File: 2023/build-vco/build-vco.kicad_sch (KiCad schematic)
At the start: 5 parts, among them M1 PMOS_OR1, M2 NMOS_OR1, M27 NMOS_OR1, M3 PMOS_OR1, M4 NMOS_OR1

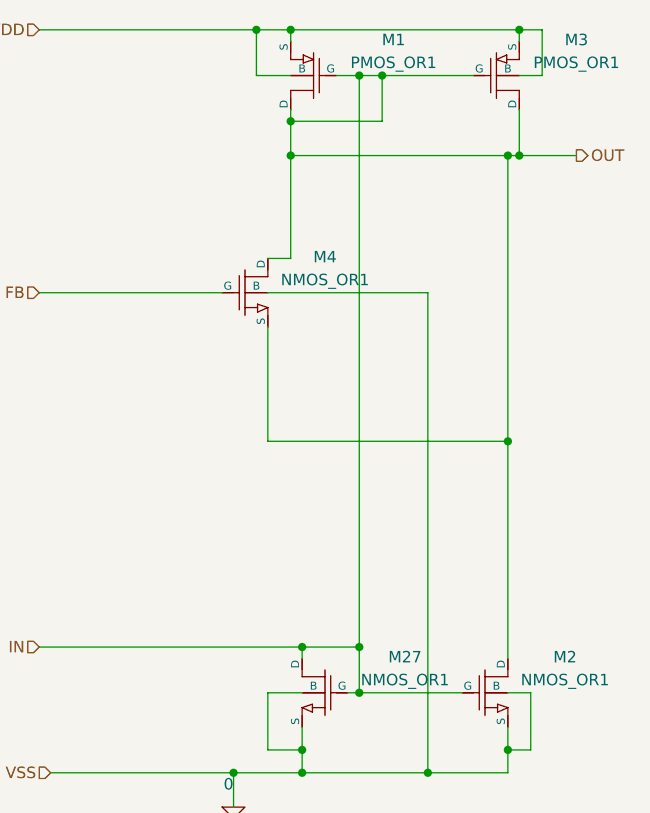
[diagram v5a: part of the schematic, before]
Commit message: 二本信号線を削った。
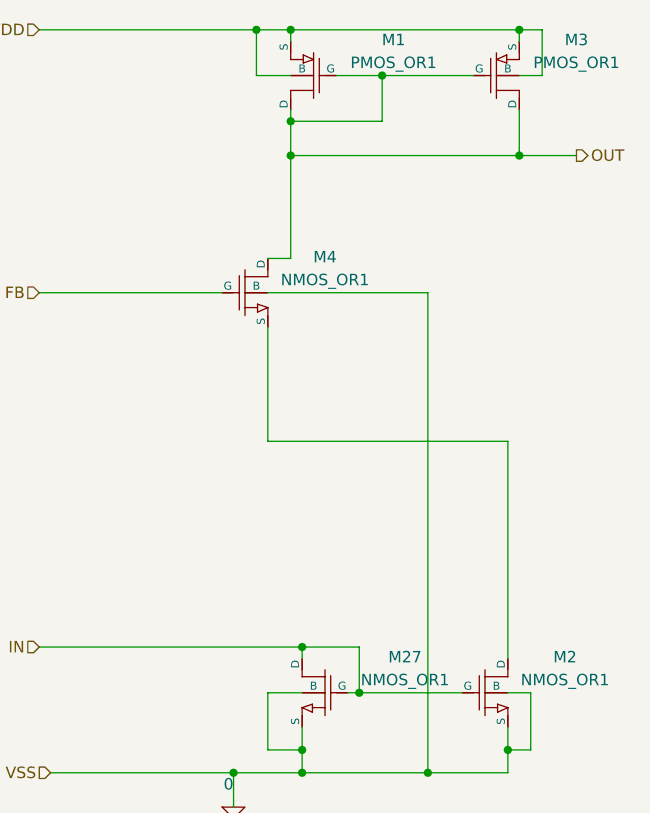
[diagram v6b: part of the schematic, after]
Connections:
- net IN: no longer M1.1 (D), M1.2 (G), M2.1 (D), M3.1 (D), M3.2 (G), M4.1 (D), M4.3 (S)
- new net: M2.1 (D), M4.3 (S)
- new net OUT: M1.1 (D), M1.2 (G), M3.1 (D), M3.2 (G), M4.1 (D)
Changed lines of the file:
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@@
   (junction (at 156.21 134.62) (diameter 0) (color 0 0 0 0)
-  )
-  (junction (at 139.7 59.69) (diameter 0) (color 0 0 0 0)
-  )
-  (junction (at 156.21 68.58) (diameter 0) (color 0 0 0 0)
-  )
-  (junction (at 156.21 100.33) (diameter 0) (color 0 0 0 0)
   )
   (junction (at 142.24 59.69) (diameter 0) (color 0 0 0 0)
@@
   )
   (junction (at 139.7 128.27) (diameter 0) (color 0 0 0 0)
-  )
-  (junction (at 139.7 123.19) (diameter 0) (color 0 0 0 0)
   )
   (junction (at 132.08 64.77) (diameter 0) (color 0 0 0 0)
@@
     (stroke (width 0) (type default))
   )
-  (wire (pts (xy 139.7 59.69) (xy 139.7 123.19))
-    (stroke (width 0) (type default))
-  )
-  (wire (pts (xy 156.21 68.58) (xy 157.48 68.58))
+  (wire (pts (xy 132.08 68.58) (xy 157.48 68.58))
     (stroke (width 0) (type default))
   )
@@
   )
   (wire (pts (xy 129.54 80.01) (xy 132.08 80.01))
-    (stroke (width 0) (type default))
-  )
-  (wire (pts (xy 137.16 59.69) (xy 139.7 59.69))
     (stroke (width 0) (type default))
   )
@@
     (stroke (width 0) (type default))
   )
-  (wire (pts (xy 139.7 59.69) (xy 142.24 59.69))
+  (wire (pts (xy 137.16 59.69) (xy 142.24 59.69))
     (stroke (width 0) (type default))
   )
@@
     (stroke (width 0) (type default))
   )
-  (wire (pts (xy 156.21 68.58) (xy 156.21 100.33))
-    (stroke (width 0) (type default))
-  )
   (wire (pts (xy 156.21 137.16) (xy 147.32 137.16))
     (stroke (width 0) (type default))
   )
-  (wire (pts (xy 132.08 68.58) (xy 156.21 68.58))
-    (stroke (width 0) (type default))
-  )

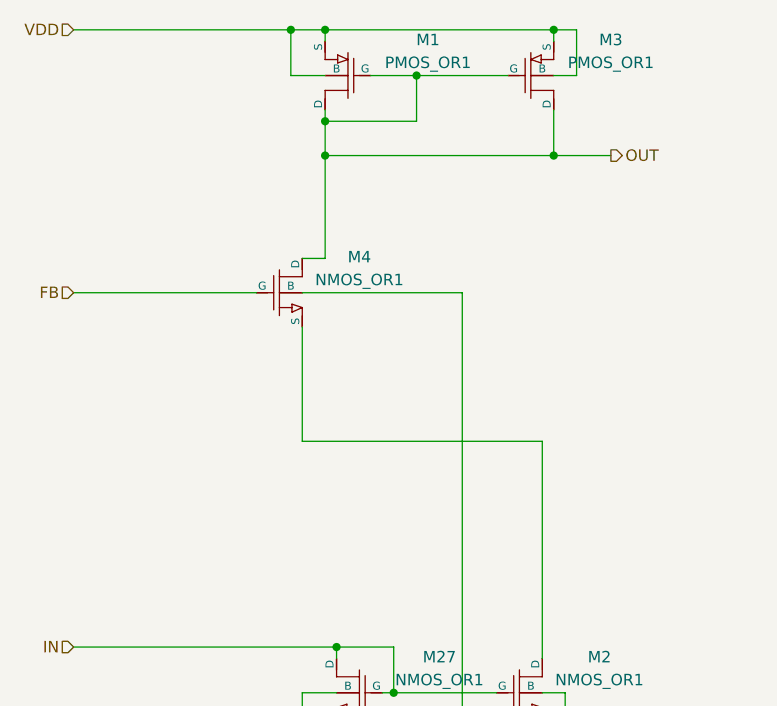
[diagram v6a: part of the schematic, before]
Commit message: PMOS x 2, NMOS x 5 で LVS は OK.
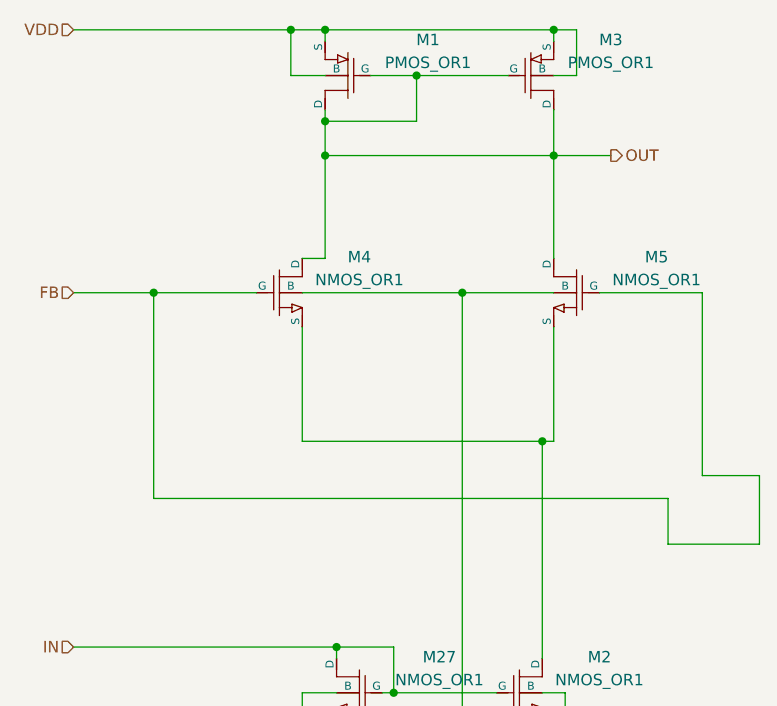
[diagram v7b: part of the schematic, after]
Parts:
- added M5: NMOS_OR1, symbol OR1Symbols:NMOS_OR1
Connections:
- net 0: now also M5.4 (B)
- net FB: now also M5.2 (G)
- net OUT: now also M5.1 (D)
- net at M2.1 (D), M4.3 (S): now also M5.3 (S)
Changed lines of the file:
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@@
   (junction (at 156.21 134.62) (diameter 0) (color 0 0 0 0)
   )
+  (junction (at 113.03 83.82) (diameter 0) (color 0 0 0 0)
+  )
+  (junction (at 147.32 83.82) (diameter 0) (color 0 0 0 0)
+  )
   (junction (at 142.24 59.69) (diameter 0) (color 0 0 0 0)
   )
@@
   (junction (at 133.35 134.62) (diameter 0) (color 0 0 0 0)
   )
+  (junction (at 156.21 100.33) (diameter 0) (color 0 0 0 0)
+  )
   (junction (at 128.27 54.61) (diameter 0) (color 0 0 0 0)
   )
@@
   (junction (at 125.73 137.16) (diameter 0) (color 0 0 0 0)
   )
+  (wire (pts (xy 147.32 83.82) (xy 157.48 83.82))
+    (stroke (width 0) (type default))
+  )
   (wire (pts (xy 104.14 54.61) (xy 128.27 54.61))
     (stroke (width 0) (type default))
@@
     (stroke (width 0) (type default))
   )
+  (wire (pts (xy 180.34 104.14) (xy 180.34 111.76))
+    (stroke (width 0) (type default))
+  )
   (wire (pts (xy 132.08 68.58) (xy 132.08 80.01))
     (stroke (width 0) (type default))
@@
     (stroke (width 0) (type default))
   )
+  (wire (pts (xy 113.03 106.68) (xy 170.18 106.68))
+    (stroke (width 0) (type default))
+  )
   (wire (pts (xy 157.48 54.61) (xy 160.02 54.61))
     (stroke (width 0) (type default))
@@
     (stroke (width 0) (type default))
   )
+  (wire (pts (xy 173.99 83.82) (xy 173.99 104.14))
+    (stroke (width 0) (type default))
+  )
   (wire (pts (xy 129.54 128.27) (xy 129.54 134.62))
     (stroke (width 0) (type default))
@@
     (stroke (width 0) (type default))
   )
+  (wire (pts (xy 162.56 83.82) (xy 173.99 83.82))
+    (stroke (width 0) (type default))
+  )
   (wire (pts (xy 125.73 137.16) (xy 133.35 137.16))
     (stroke (width 0) (type default))
@@
     (stroke (width 0) (type default))
   )
+  (wire (pts (xy 170.18 111.76) (xy 170.18 106.68))
+    (stroke (width 0) (type default))
+  )
   (wire (pts (xy 132.08 64.77) (xy 132.08 68.58))
     (stroke (width 0) (type default))
   )
-  (wire (pts (xy 104.14 83.82) (xy 124.46 83.82))
+  (wire (pts (xy 104.14 83.82) (xy 113.03 83.82))
     (stroke (width 0) (type default))
   )
@@
     (stroke (width 0) (type default))
   )
+  (wire (pts (xy 157.48 87.63) (xy 157.48 100.33))
+    (stroke (width 0) (type default))
+  )
   (wire (pts (xy 157.48 68.58) (xy 163.83 68.58))
     (stroke (width 0) (type default))
@@
     (stroke (width 0) (type default))
   )
+  (wire (pts (xy 113.03 106.68) (xy 113.03 83.82))
+    (stroke (width 0) (type default))
+  )
   (wire (pts (xy 157.48 59.69) (xy 160.02 59.69))
     (stroke (width 0) (type default))
   )
+  (wire (pts (xy 180.34 111.76) (xy 170.18 111.76))
+    (stroke (width 0) (type default))
+  )
   (wire (pts (xy 142.24 59.69) (xy 142.24 64.77))
     (stroke (width 0) (type default))
@@
     (stroke (width 0) (type default))
   )
+  (wire (pts (xy 157.48 68.58) (xy 157.48 80.01))
+    (stroke (width 0) (type default))
+  )
+  (wire (pts (xy 173.99 104.14) (xy 180.34 104.14))
+    (stroke (width 0) (type default))
+  )
   (wire (pts (xy 142.24 59.69) (xy 152.4 59.69))
     (stroke (width 0) (type default))
@@
     (stroke (width 0) (type default))
   )
+  (wire (pts (xy 156.21 100.33) (xy 157.48 100.33))
+    (stroke (width 0) (type default))
+  )
   (wire (pts (xy 132.08 63.5) (xy 132.08 64.77))
+    (stroke (width 0) (type default))
+  )
+  (wire (pts (xy 113.03 83.82) (xy 124.46 83.82))
     (stroke (width 0) (type default))
   )
@@
         )
       )
+    )
+  )
+  (symbol (lib_name "NMOS_OR1_3") (lib_id "OR1Symbols:NMOS_OR1") (at 162.56 83.82 0) (mirror y) (unit 1)
+    (in_bom yes) (on_board yes) (dnp no) (fields_autoplaced)
+    (property "Reference" "M5" (at 168.91 79.8577 0)
+      (effects (font (size 1.27 1.27)))
+    )
+    (property "Value" "NMOS_OR1" (at 168.91 82.3977 0)
+      (effects (font (size 1.27 1.27)))
+    )
+    (property "Footprint" "" (at 162.56 83.82 0)
+      (effects (font (size 1.27 1.27)) hide)
+    )
+    (property "Datasheet" "" (at 162.56 83.82 0)
+      (effects (font (size 1.27 1.27)) hide)
+    )
+    (property "Sim.Pins" "1=1 2=2 3=3 4=4" (at 162.56 83.82 0)
+      (effects (font (size 1.27 1.27)) hide)
+    )
+    (property "Sim.Device" "SPICE" (at 153.67 88.9 0)
+      (effects (font (size 1.27 1.27)) (justify left) hide)
+    )
+    (property "Sim.Params" "type=\"M\" model=\"NMOS_OR1 l=1u w=2u\" lib=\"\"" (at 162.56 83.82 0)
+      (effects (font (size 1.27 1.27)) hide)
+    )
+    (pin "1")
+    (pin "2")
+    (pin "3")
+    (pin "4")
+    (instances
+      (project "build-vco"
+        (path "/178e7a69-f569-4b69-ab89-e6b9cdb6309f"
+          (reference "M5") (unit 1)
+        )
+      )

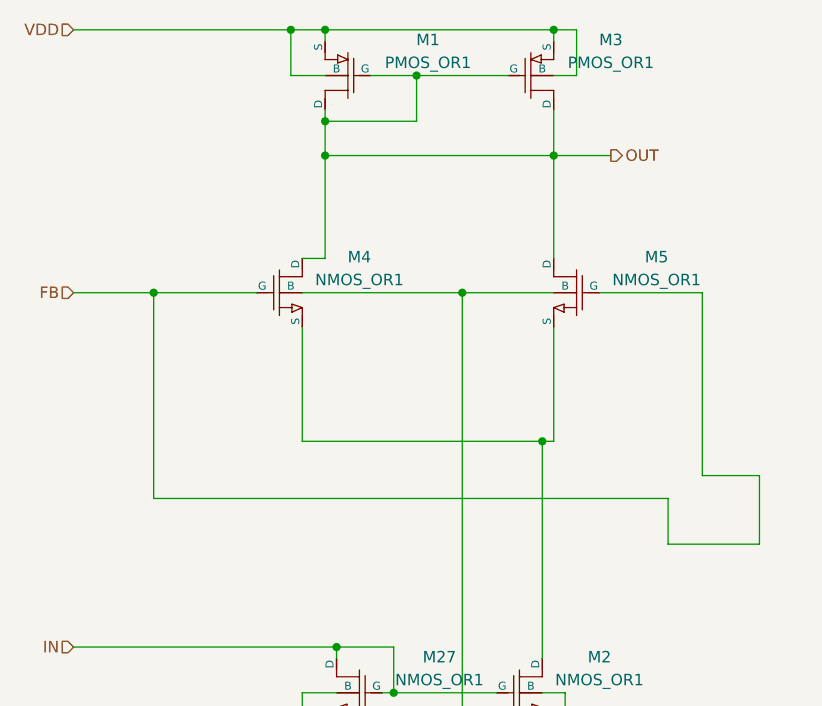
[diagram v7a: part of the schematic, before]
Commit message: FB を削除して OUT を移動した。LVS は通った。
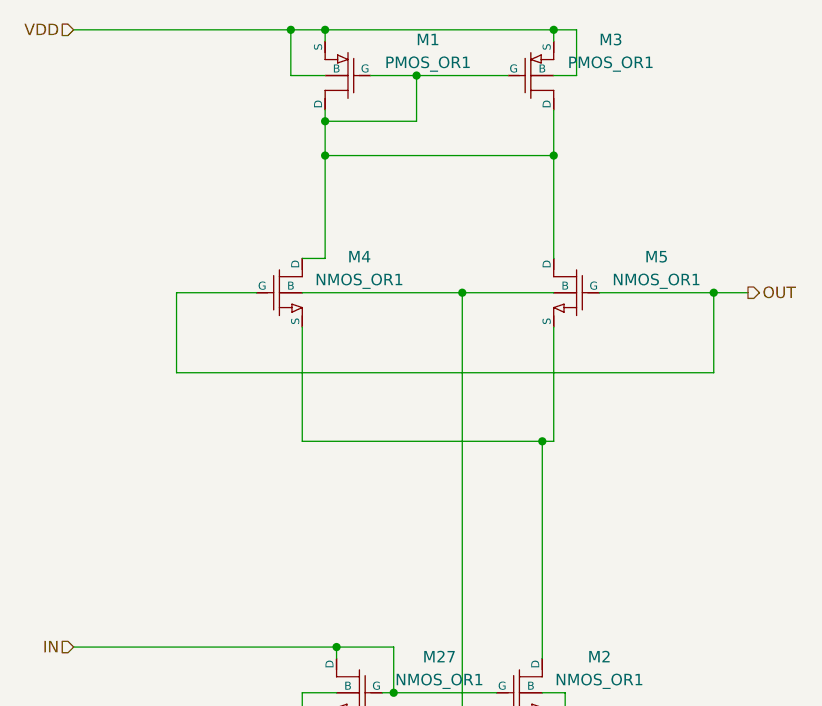
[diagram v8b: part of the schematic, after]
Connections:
- net FB is gone; now on net OUT: M4.2 (G), M5.2 (G)
- net OUT: no longer M1.1 (D), M1.2 (G), M3.1 (D), M3.2 (G), M4.1 (D), M5.1 (D)
- new net: M1.1 (D), M1.2 (G), M3.1 (D), M3.2 (G), M4.1 (D), M5.1 (D)
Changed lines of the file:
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@@
   (junction (at 156.21 134.62) (diameter 0) (color 0 0 0 0)
   )
-  (junction (at 113.03 83.82) (diameter 0) (color 0 0 0 0)
+  (junction (at 175.26 83.82) (diameter 0) (color 0 0 0 0)
   )
   (junction (at 147.32 83.82) (diameter 0) (color 0 0 0 0)
@@
     (stroke (width 0) (type default))
   )
-  (wire (pts (xy 180.34 104.14) (xy 180.34 111.76))
-    (stroke (width 0) (type default))
-  )
   (wire (pts (xy 132.08 68.58) (xy 132.08 80.01))
     (stroke (width 0) (type default))
@@
     (stroke (width 0) (type default))
   )
-  (wire (pts (xy 113.03 106.68) (xy 170.18 106.68))
-    (stroke (width 0) (type default))
-  )
   (wire (pts (xy 157.48 54.61) (xy 160.02 54.61))
     (stroke (width 0) (type default))
@@
     (stroke (width 0) (type default))
   )
-  (wire (pts (xy 173.99 83.82) (xy 173.99 104.14))
-    (stroke (width 0) (type default))
-  )
   (wire (pts (xy 129.54 128.27) (xy 129.54 134.62))
     (stroke (width 0) (type default))
@@
     (stroke (width 0) (type default))
   )
-  (wire (pts (xy 162.56 83.82) (xy 173.99 83.82))
+  (wire (pts (xy 115.57 92.71) (xy 115.57 83.82))
     (stroke (width 0) (type default))
   )
@@
     (stroke (width 0) (type default))
   )
+  (wire (pts (xy 175.26 83.82) (xy 179.07 83.82))
+    (stroke (width 0) (type default))
+  )
   (wire (pts (xy 129.54 134.62) (xy 133.35 134.62))
     (stroke (width 0) (type default))
@@
     (stroke (width 0) (type default))
   )
-  (wire (pts (xy 170.18 111.76) (xy 170.18 106.68))
-    (stroke (width 0) (type default))
-  )
   (wire (pts (xy 132.08 64.77) (xy 132.08 68.58))
     (stroke (width 0) (type default))
   )
-  (wire (pts (xy 104.14 83.82) (xy 113.03 83.82))
+  (wire (pts (xy 115.57 83.82) (xy 124.46 83.82))
     (stroke (width 0) (type default))
   )
@@
     (stroke (width 0) (type default))
   )
+  (wire (pts (xy 162.56 83.82) (xy 175.26 83.82))
+    (stroke (width 0) (type default))
+  )
   (wire (pts (xy 156.21 100.33) (xy 156.21 124.46))
     (stroke (width 0) (type default))
@@
     (stroke (width 0) (type default))
   )
-  (wire (pts (xy 157.48 68.58) (xy 163.83 68.58))
+  (wire (pts (xy 175.26 83.82) (xy 175.26 92.71))
     (stroke (width 0) (type default))
   )
@@
     (stroke (width 0) (type default))
   )
+  (wire (pts (xy 175.26 92.71) (xy 115.57 92.71))
+    (stroke (width 0) (type default))
+  )
   (wire (pts (xy 129.54 100.33) (xy 156.21 100.33))
     (stroke (width 0) (type default))
   )
-  (wire (pts (xy 113.03 106.68) (xy 113.03 83.82))
-    (stroke (width 0) (type default))
-  )
   (wire (pts (xy 157.48 59.69) (xy 160.02 59.69))
     (stroke (width 0) (type default))
   )
-  (wire (pts (xy 180.34 111.76) (xy 170.18 111.76))
-    (stroke (width 0) (type default))
-  )
   (wire (pts (xy 142.24 59.69) (xy 142.24 64.77))
     (stroke (width 0) (type default))
   )
+  (wire (pts (xy 157.48 68.58) (xy 157.48 80.01))
+    (stroke (width 0) (type default))
+  )
   (wire (pts (xy 133.35 123.19) (xy 139.7 123.19))
     (stroke (width 0) (type default))
@@
     (stroke (width 0) (type default))
   )
-  (wire (pts (xy 157.48 68.58) (xy 157.48 80.01))
-    (stroke (width 0) (type default))
-  )
-  (wire (pts (xy 173.99 104.14) (xy 180.34 104.14))
-    (stroke (width 0) (type default))
-  )
   (wire (pts (xy 142.24 59.69) (xy 152.4 59.69))
     (stroke (width 0) (type default))
@@
   )
   (wire (pts (xy 132.08 63.5) (xy 132.08 64.77))
-    (stroke (width 0) (type default))
-  )
-  (wire (pts (xy 113.03 83.82) (xy 124.46 83.82))
     (stroke (width 0) (type default))
   )
@@
     (effects (font (size 1.27 1.27)) (justify right))
   )
-  (hierarchical_label "OUT" (shape output) (at 163.83 68.58 0) (fields_autoplaced)
+  (hierarchical_label "OUT" (shape output) (at 179.07 83.82 0) (fields_autoplaced)
     (effects (font (size 1.27 1.27)) (justify left))
   )
@@
     (effects (font (size 1.27 1.27)) (justify right))
   )
-  (hierarchical_label "FB" (shape input) (at 104.14 83.82 180) (fields_autoplaced)
-    (effects (font (size 1.27 1.27)) (justify right))
-  )
